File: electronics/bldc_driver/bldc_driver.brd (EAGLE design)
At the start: 100 x 80 mm, 33 parts, among them Q1 MOSFET-N, Q2 MOSFET-N, Q3 MOSFET-N, Q4 MOSFET-N, Q5 MOSFET-N, Q6 MOSFET-N, X1 LOGIC, X2 POWER

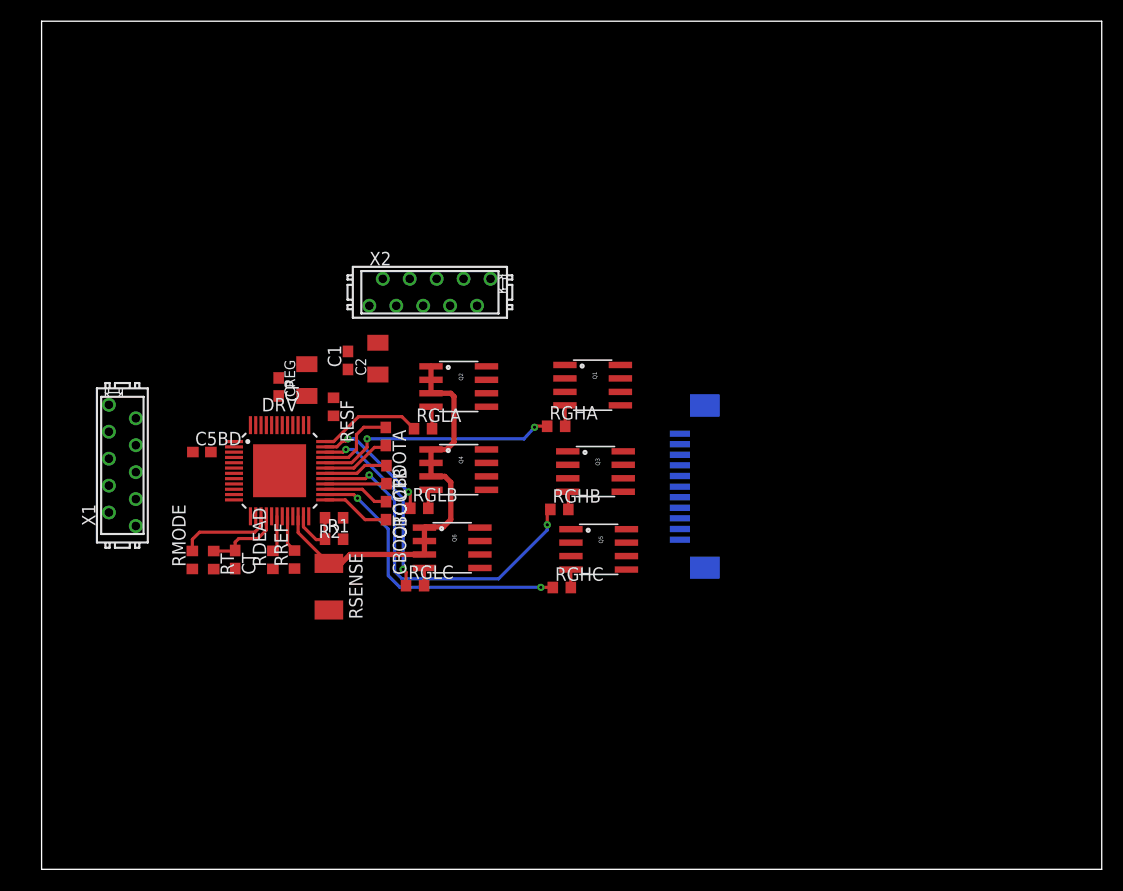
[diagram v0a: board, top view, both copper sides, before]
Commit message: Routed motor driver board
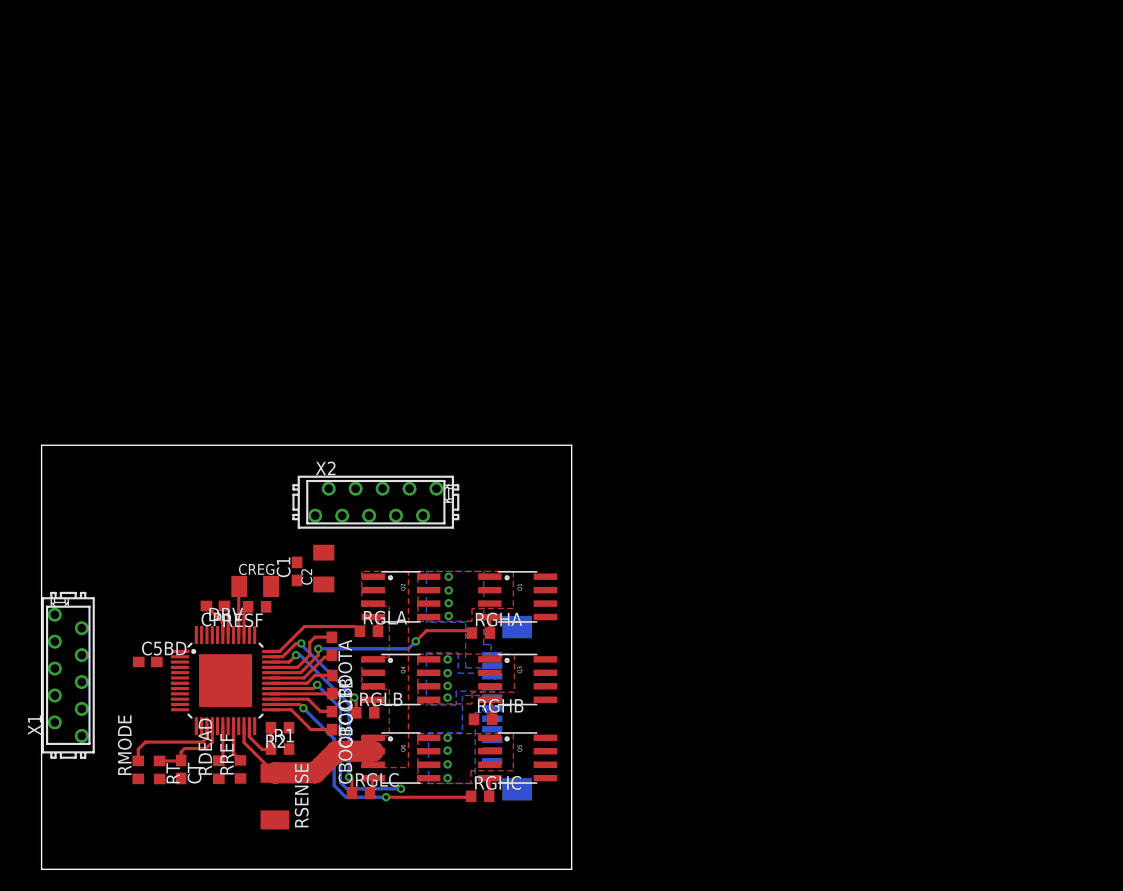
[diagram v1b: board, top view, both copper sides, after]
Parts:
- moved MOTOR 27.4 mm to (37.7, 15.2)
- moved CP 21.5 mm to (16.4, 24.8), turned to 180 degrees
- moved Q1 21.2 mm to (44.9, 25.7)
- moved RGHC 21.2 mm to (41.4, 6.88)
- moved Q5 21.1 mm to (44.9, 10.5)
- moved RGHB 21.1 mm to (41.6, 14.2)
- moved Q3 21.0 mm to (44.9, 17.9)
- moved RGHA 20.8 mm to (41.4, 22.3)
- moved Q2 20.6 mm to (33.9, 25.7)
- moved Q4 20.5 mm to (33.9, 17.9)
- moved C1 20.5 mm to (24.1, 28.1)
- moved RT 20.4 mm to (11.1, 9.37)
- moved C2 20.4 mm to (26.6, 28.4)
- moved C5BD 20.4 mm to (10.0, 19.6)
- moved DRV 20.4 mm to (17.4, 17.8)
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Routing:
- net LSS: track 40.1 -> 15.8 mm
- net GHB: track 33.6 -> 20.6 mm
- net N$8: track 0.00 -> 4.58 mm
- net N$11: track 0.00 -> 3.38 mm
- net N$10: track 0.00 -> 3.04 mm
- net ESF: track 0.00 -> 2.82 mm
- net GHC: track 27.7 -> 25.1 mm
- net GHA: track 22.9 -> 21.0 mm
- net N$4: track 1.84 -> 1.25 mm
- net SA: vias 0 -> 4
- net SC: vias 0 -> 4
- net SB: vias 0 -> 4
- added copper zone on layer 1, net LSS
- added copper zone on layer 1, net SA
- added copper zone on layer 16, net SA
- added copper zone on layer 1, net SB
- added copper zone on layer 16, net SB
- added copper zone on layer 1, net SC
- added copper zone on layer 16, net SC
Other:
- board size 100 x 80 mm -> 50 x 40 mm

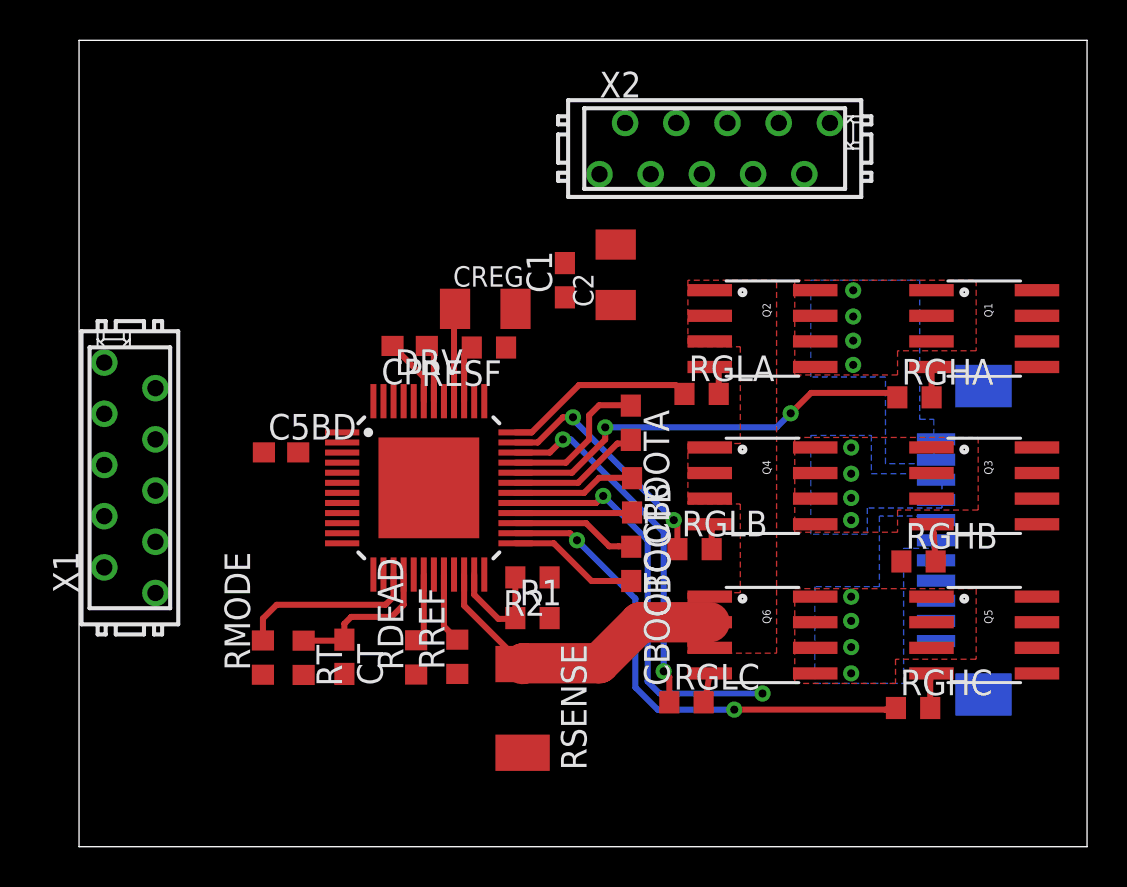
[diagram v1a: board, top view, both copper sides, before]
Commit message: Routed motor driver board
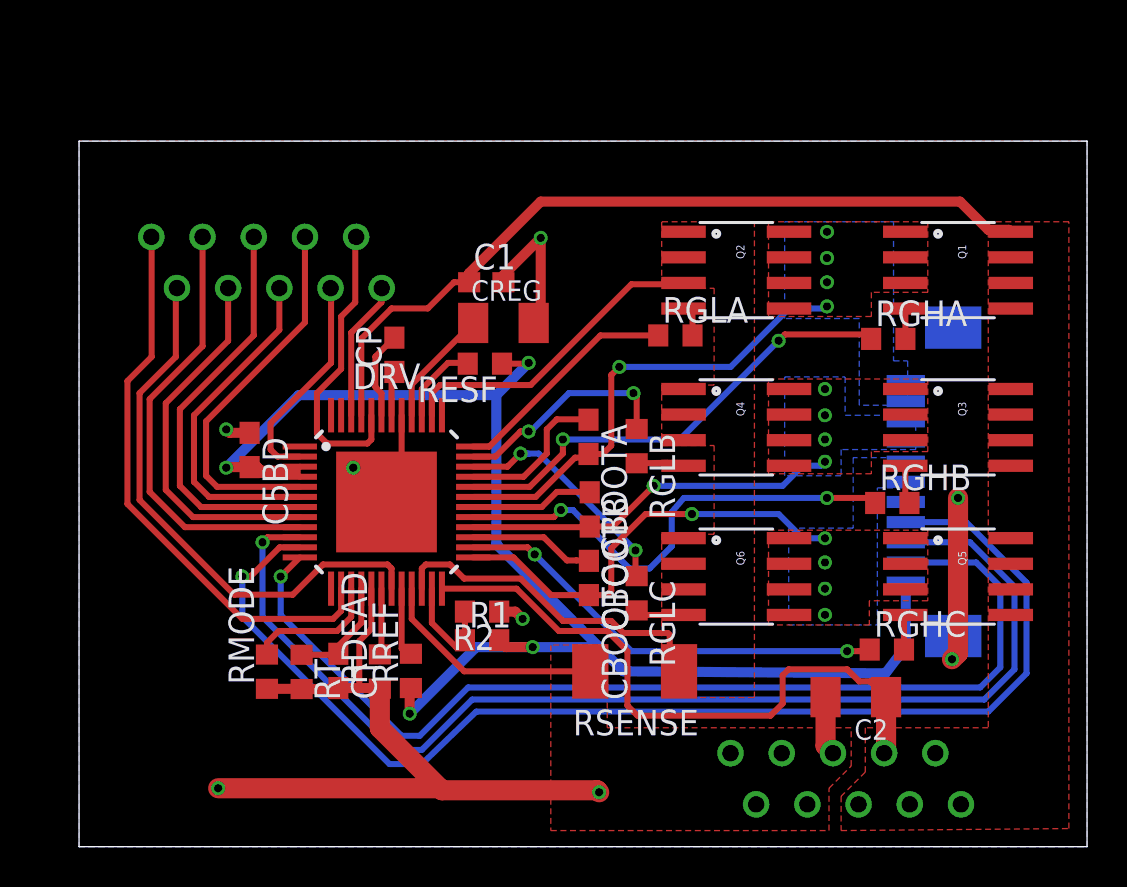
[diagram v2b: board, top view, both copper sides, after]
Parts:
- moved X2 31.9 mm to (38.0, 3.37), flipped to the bottom, turned to 180 degrees
- moved C2 24.1 mm to (38.5, 7.42), turned to 180 degrees
- moved X1 12.7 mm to (9.30, 29.0), flipped to the bottom, turned to 0 degrees
- moved RGLC 5.95 mm to (27.7, 12.6), turned to 270 degrees
- moved RGLB 5.86 mm to (27.7, 19.9), turned to 270 degrees
- moved RSENSE 5.86 mm to (27.6, 8.70), turned to 180 degrees
- moved C1 3.90 mm to (20.2, 28.0), turned to 0 degrees
- moved MOTOR 3.26 mm to (36.2, 18.1)
- moved Q1 3.18 mm to (43.6, 28.6)
- moved Q2 3.18 mm to (32.6, 28.6)
- moved Q3 3.18 mm to (43.6, 20.8)
- moved Q4 3.18 mm to (32.6, 20.8)
- moved RGHA 3.18 mm to (40.1, 25.2)
- moved Q5 3.18 mm to (43.6, 13.4)
- moved Q6 3.18 mm to (32.6, 13.4)
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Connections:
- net BRAKE: now also X1.4; no longer X1.5
- net CSOUT: now also X1.2; no longer X1.8
- net DIR: now also X1.3; no longer X1.6
- net FF1: now also X1.6; no longer X1.3
- net FF2: now also X1.7; no longer X1.2
- net PWM: now also X1.1; no longer X1.7
- net RESET: now also X1.8; no longer X1.1
- net TACHO: now also X1.5; no longer X1.4
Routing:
- net GND: track 0.06 -> 76.5 mm, vias 0 -> 8
- net +12V: track 0.00 -> 71.2 mm
- net +5V: track 0.00 -> 70.7 mm, vias 0 -> 4
- net H2: track 0.00 -> 60.9 mm, vias 0 -> 1
- net H1: track 0.00 -> 57.7 mm, vias 0 -> 1
- net H3: track 0.00 -> 52.3 mm, vias 0 -> 1
- net PWM: track 0.00 -> 28.0 mm
- net CSOUT: track 0.00 -> 27.4 mm
- net DIR: track 0.00 -> 21.9 mm
- net TACHO: track 0.00 -> 20.3 mm
- net FF2: track 0.00 -> 18.8 mm
- net BRAKE: track 0.00 -> 18.5 mm
- net FF1: track 0.00 -> 16.9 mm
- net SA: track 6.60 -> 23.5 mm, vias 4 -> 5
- net LSS: track 15.8 -> 32.7 mm
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- added copper zone on layer 1, net +12V
- added copper zone on layer 1, net GND
- added copper zone on layer 16, net GND
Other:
- board size 50 x 40 mm -> 50 x 35 mm

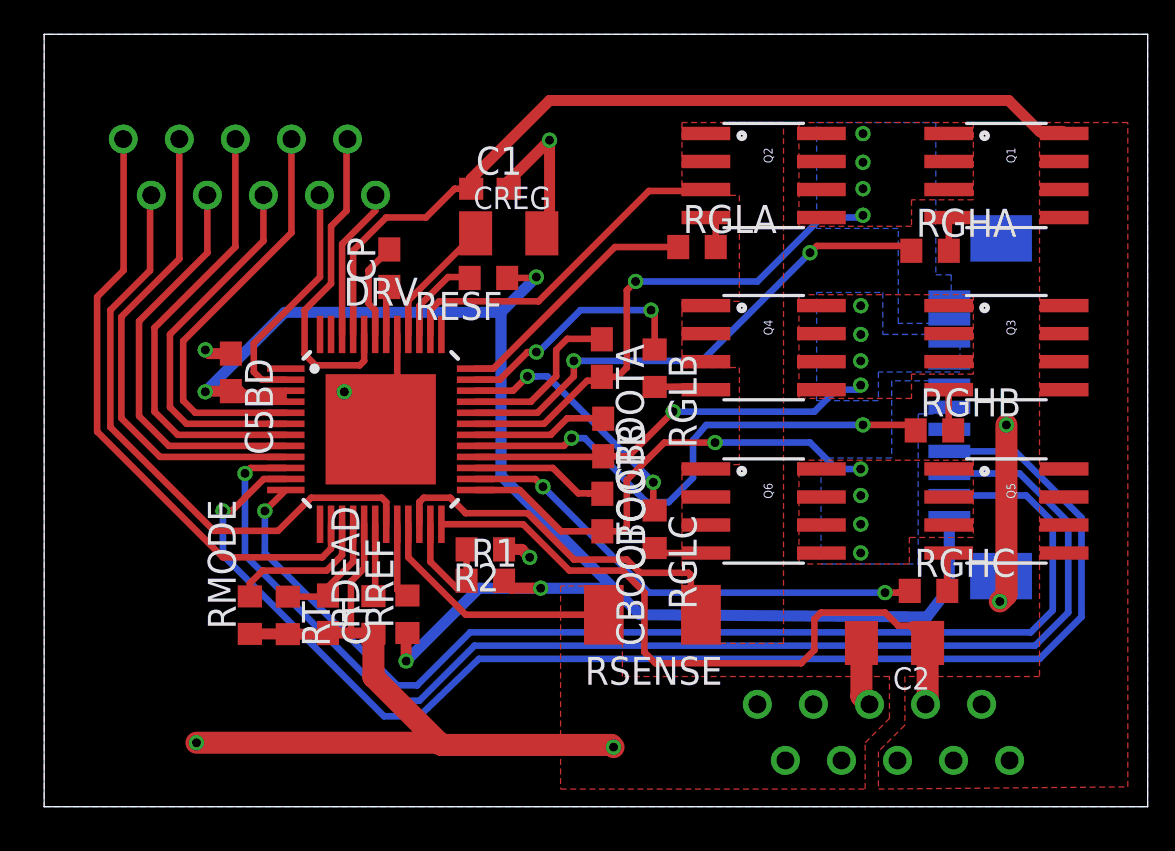
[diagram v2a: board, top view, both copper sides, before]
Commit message: Adjusted some mechanical parts and added initial electronic and electrical parts
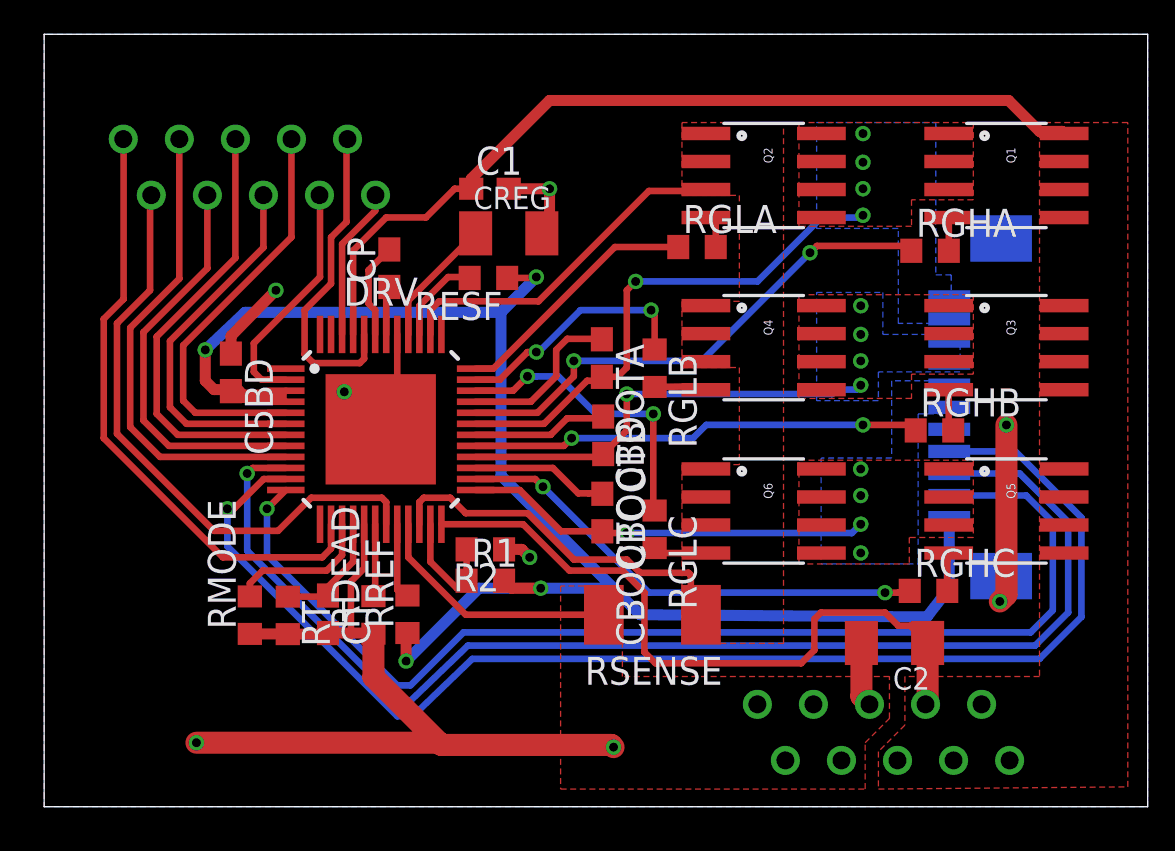
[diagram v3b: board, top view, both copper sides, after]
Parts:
- moved CBOOTB 0.10 mm to (25.3, 16.8)
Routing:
- net GHB: track 24.0 -> 20.5 mm
- net SC: track 21.6 -> 18.5 mm
- net GLC: track 12.4 -> 14.2 mm
- net SB: track 18.8 -> 19.7 mm
- net GND: track 76.5 -> 75.7 mm
- net +5V: track 70.7 -> 71.5 mm
- net H2: track 60.9 -> 60.4 mm

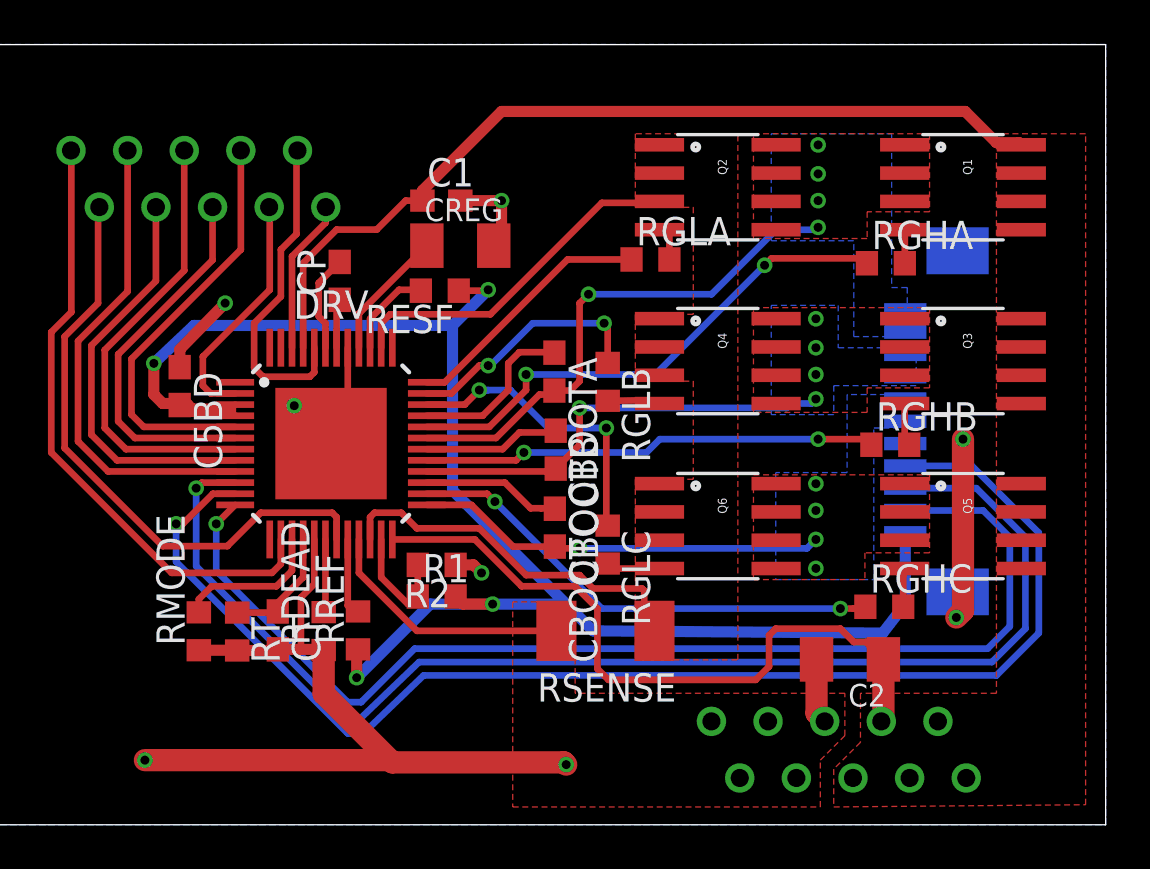
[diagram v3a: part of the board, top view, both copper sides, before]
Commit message: Did some motor driver board routing
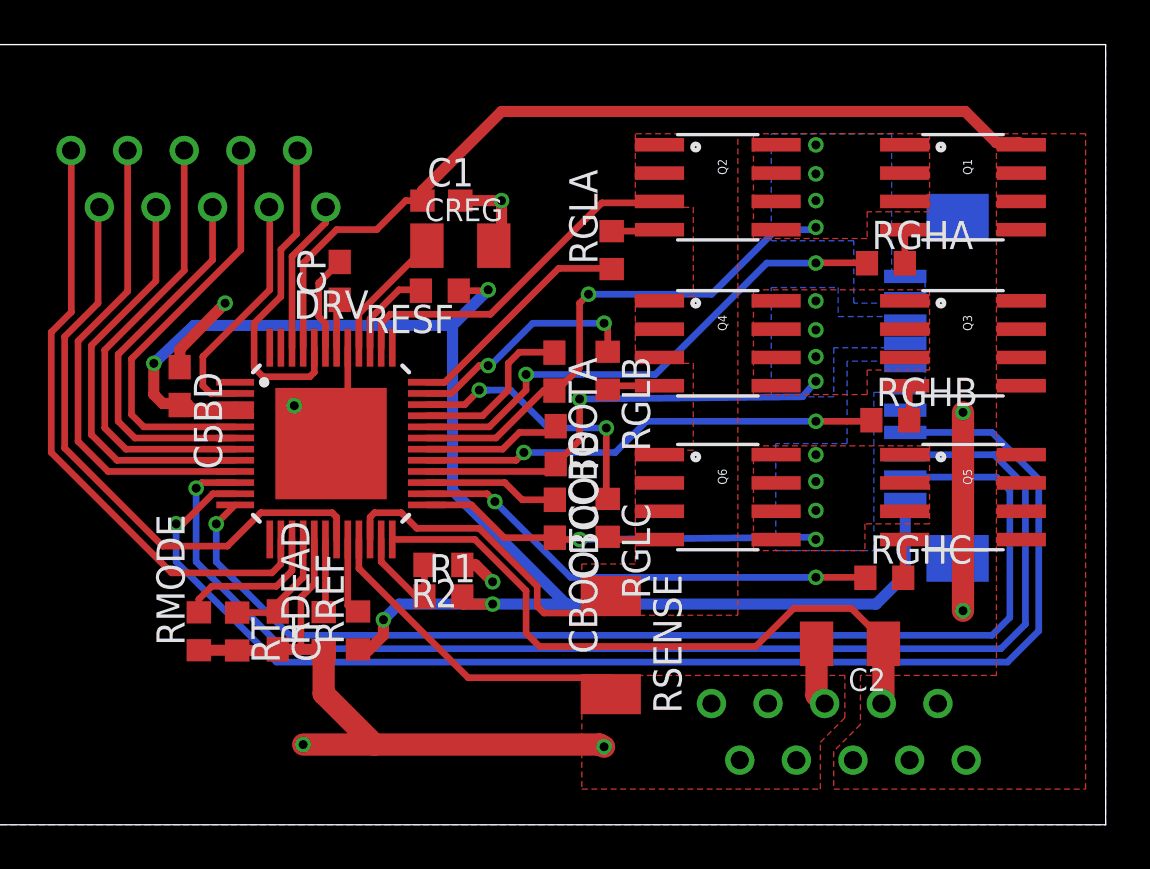
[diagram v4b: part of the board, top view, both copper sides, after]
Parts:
- moved RGLA 1.79 mm to (27.8, 25.8), turned to 90 degrees
- moved MOTOR 1.50 mm to (36.2, 19.6)
- moved RGHC 1.30 mm to (40.1, 11.1)
- moved Q5 1.30 mm to (43.6, 14.7)
- moved Q6 1.30 mm to (32.6, 14.7)
- moved RGLC 1.20 mm to (27.7, 13.8)
- moved RGHB 1.10 mm to (40.3, 18.1)
- moved Q3 0.80 mm to (43.6, 21.6)
- moved Q4 0.80 mm to (32.6, 21.6)
- moved X2 0.80 mm to (38.0, 4.17)
- moved C2 0.70 mm to (38.5, 8.12)
- moved RSENSE 0.68 mm to (27.8, 8.06), turned to 270 degrees
- moved RGLB 0.50 mm to (27.7, 20.4)
- moved CBOOTC 0.40 mm to (25.3, 13.7)
- moved R1 0.30 mm to (20.3, 10.2)
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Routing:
- net GND: track 75.7 -> 73.1 mm
- net LSS: track 32.7 -> 30.3 mm
- net +12V: track 71.2 -> 69.1 mm
- net H3: track 52.3 -> 50.8 mm
- net GLC: track 14.2 -> 12.8 mm
- net N$2: track 1.73 -> 3.04 mm
- net GLA: track 11.5 -> 10.4 mm
- net H1: track 57.4 -> 56.6 mm
- net H2: track 60.4 -> 59.7 mm
- net GHC: track 21.8 -> 21.2 mm
- net +5V: track 71.5 -> 71.0 mm
- net VDSTH: track 5.96 -> 5.43 mm
- net GLB: track 11.2 -> 10.7 mm
